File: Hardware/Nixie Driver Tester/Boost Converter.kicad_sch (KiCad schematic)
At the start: 6 parts, among them Q1 MMBT2222A, Q2 MMBT2907ALT1G, Q3 FDD7N25LZTM

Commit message: Switch mode 3.3V and SMD inductor
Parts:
- added C6: 100nF, Capacitor_SMD:C_0805_2012Metric, symbol Device:C
- L1: footprint Inductor_:Bourns RLB1014 -> Inductor_SMD:L_Wuerth_WE-PD-Typ-LS
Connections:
- net GND: now also C6.1
- net VBUS: now also C6.2
- net Gate Drive: now reaches Q1.2 (E), Q2.2 (E), Q3.1 (G)
- net Boost Src: now reaches D1.2 (A), L1.2, Q3.2 (D)
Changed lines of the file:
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@@
 	(paper "A4")
+	(junction
+		(at 93.98 58.42)
+		(diameter 0)
+		(color 0 0 0 0)
+	)
 	(junction
 		(at 101.6 88.9)
@@
 	)
 	(junction
-		(at 93.98 88.9)
+		(at 91.44 88.9)
 		(diameter 0)
 		(color 0 0 0 0)
@@
 	(wire
 		(pts
+			(xy 93.98 58.42) (xy 88.9 58.42)
+		)
+		(stroke
+			(width 0)
+			(type default)
+		)
+	)
+	(wire
+		(pts
 			(xy 101.6 88.9) (xy 111.76 88.9)
 		)
@@
 	(wire
 		(pts
+			(xy 93.98 40.64) (xy 93.98 43.18)
+		)
+		(stroke
+			(width 0)
+			(type default)
+		)
+	)
+	(wire
+		(pts
 			(xy 121.92 101.6) (xy 152.4 101.6)
 		)
@@
 	(wire
 		(pts
-			(xy 88.9 88.9) (xy 93.98 88.9)
-		)
-		(stroke
-			(width 0)
-			(type default)
-		)
-	)
-	(wire
-		(pts
-			(xy 93.98 88.9) (xy 93.98 101.6)
+			(xy 88.9 88.9) (xy 91.44 88.9)
+		)
+		(stroke
+			(width 0)
+			(type default)
+		)
+	)
+	(wire
+		(pts
+			(xy 91.44 88.9) (xy 91.44 101.6)
 		)
 		(stroke
@@
 	(wire
 		(pts
+			(xy 93.98 50.8) (xy 93.98 58.42)
+		)
+		(stroke
+			(width 0)
+			(type default)
+		)
+	)
+	(wire
+		(pts
 			(xy 101.6 63.5) (xy 101.6 71.12)
 		)
@@
 	(wire
 		(pts
-			(xy 106.68 58.42) (xy 88.9 58.42)
+			(xy 106.68 58.42) (xy 93.98 58.42)
 		)
 		(stroke
@@
 	(wire
 		(pts
-			(xy 93.98 88.9) (xy 93.98 76.2)
-		)
-		(stroke
-			(width 0)
-			(type default)
+			(xy 91.44 101.6) (xy 93.98 101.6)
+		)
+		(stroke
+			(width 0)
+			(type default)
+		)
+	)
+	(wire
+		(pts
+			(xy 91.44 88.9) (xy 91.44 76.2)
+		)
+		(stroke
+			(width 0)
+			(type default)
+		)
+	)
+	(wire
+		(pts
+			(xy 91.44 76.2) (xy 93.98 76.2)
+		)
+		(stroke
+			(width 0)
+			(type default)
+		)
+	)
+	(label "Gate Drive"
+		(at 101.6 93.98 0)
+		(effects
+			(font
+				(size 1.27 1.27)
+			)
+			(justify left bottom)
+		)
+	)
+	(label "Boost Src"
+		(at 121.92 68.58 0)
+		(effects
+			(font
+				(size 1.27 1.27)
+			)
+			(justify left bottom)
 		)
 	)
@@
 		(dnp no)
 		(fields_autoplaced yes)
-		(property "Reference" "#PWR04"
+		(property "Reference" "#PWR06"
 			(at 101.6 113.03 0)
 			(hide yes)
@@
 			(project "Nixie Driver Tester"
 				(path "/c2082ee6-4c2e-4b3c-b2d7-410eae192cfe/f65193b1-af2e-4613-8eac-c37ef85f5db5"
-					(reference "#PWR04")
+					(reference "#PWR06")
 					(unit 1)
 				)
@@
 		(dnp no)
 		(fields_autoplaced yes)
-		(property "Reference" "#PWR06"
+		(property "Reference" "#PWR07"
 			(at 121.92 113.03 0)
 			(hide yes)
@@
 			(project "Nixie Driver Tester"
 				(path "/c2082ee6-4c2e-4b3c-b2d7-410eae192cfe/f65193b1-af2e-4613-8eac-c37ef85f5db5"
-					(reference "#PWR06")
+					(reference "#PWR07")
+					(unit 1)
+				)
+			)
+		)
+	)
+	(symbol
+		(lib_id "Device:C")
+		(at 93.98 46.99 0)
+		(unit 1)
+		(body_style 1)
+		(exclude_from_sim no)
+		(in_bom yes)
+		(on_board yes)
+		(in_pos_files yes)
+		(dnp no)
+		(fields_autoplaced yes)
+		(property "Reference" "C6"
+			(at 97.79 45.7199 0)
+			(show_name no)
+			(do_not_autoplace no)
+			(effects
+				(font
+					(size 1.27 1.27)
+				)
+				(justify left)
+			)
+		)
+		(property "Value" "100nF"
+			(at 97.79 48.2599 0)
+			(show_name no)
+			(do_not_autoplace no)
+			(effects
+				(font
+					(size 1.27 1.27)
+				)
+				(justify left)
+			)
+		)
+		(property "Footprint" "Capacitor_SMD:C_0805_2012Metric"
+			(at 94.9452 50.8 0)
+			(hide yes)
+			(show_name no)
+			(do_not_autoplace no)
+			(effects
+				(font
+					(size 1.27 1.27)
+				)
+			)
+		)
+		(property "Datasheet" ""
+			(at 93.98 46.99 0)
+			(hide yes)
+			(show_name no)
+			(do_not_autoplace no)
+			(effects
+				(font
+					(size 1.27 1.27)
+				)
+			)
+		)
+		(property "Description" "Unpolarized capacitor"
+			(at 93.98 46.99 0)
+			(hide yes)
+			(show_name no)
+			(do_not_autoplace no)
+			(effects
+				(font
+					(size 1.27 1.27)
+				)
+			)
+		)
+		(pin "1"
+		)
+		(pin "2"
+		)
+		(instances
+			(project "Nixie Driver Tester"
+				(path "/c2082ee6-4c2e-4b3c-b2d7-410eae192cfe/f65193b1-af2e-4613-8eac-c37ef85f5db5"
+					(reference "C6")
 					(unit 1)
 				)
@@
 			)
 		)
-		(property "Footprint" "Inductor_:Bourns RLB1014"
+		(property "Footprint" "Inductor_SMD:L_Wuerth_WE-PD-Typ-LS"
 			(at 110.49 58.42 0)
 			(hide yes)
@@
 					(unit 1)
 				)
+			)
+		)
+	)
+	(symbol
+		(lib_id "power:GND")
+		(at 93.98 40.64 180)
+		(unit 1)
+		(body_style 1)
+		(exclude_from_sim no)
+		(in_bom yes)
+		(on_board yes)
+		(in_pos_files yes)
+		(dnp no)
+		(fields_autoplaced yes)
+		(property "Reference" "#PWR026"
+			(at 93.98 34.29 0)
+			(hide yes)
+			(show_name no)
+			(do_not_autoplace no)
+			(effects
+				(font
+					(size 1.27 1.27)
+				)
+			)
+		)
+		(property "Value" "GND"
+			(at 93.98 35.56 0)
+			(show_name no)
+			(do_not_autoplace no)
+			(effects
+				(font
+					(size 1.27 1.27)
+				)
+			)
+		)
+		(property "Footprint" ""
+			(at 93.98 40.64 0)
+			(hide yes)
+			(show_name no)
+			(do_not_autoplace no)
+			(effects
+				(font
+					(size 1.27 1.27)
+				)
+			)
+		)
+		(property "Datasheet" ""
+			(at 93.98 40.64 0)
+			(hide yes)
+			(show_name no)
+			(do_not_autoplace no)
+			(effects
+				(font
+					(size 1.27 1.27)
+				)
+			)
+		)
+		(property "Description" "Power symbol creates a global label with name \"GND\" , ground"
+			(at 93.98 40.64 0)
+			(hide yes)
+			(show_name no)
+			(do_not_autoplace no)
+			(effects
+				(font
+					(size 1.27 1.27)
+				)
+			)
+		)
+		(pin "1"
+		)
+		(instances
+			(project "Nixie Driver Tester"
+				(path "/c2082ee6-4c2e-4b3c-b2d7-410eae192cfe/f65193b1-af2e-4613-8eac-c37ef85f5db5"
+					(reference "#PWR026")
+					(unit 1)
+				)

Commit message: Added test points
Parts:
- added TP3: PWM, TestPoint:TestPoint_Keystone_5015_Micro_Mini, symbol Connector:TestPoint
- added TP4: VNN, TestPoint:TestPoint_Keystone_5015_Micro_Mini, symbol Connector:TestPoint
- renumbered C6 to C2, C2 to C3
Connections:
- net 180V: now also TP4.1
- net PWM: now also TP3.1
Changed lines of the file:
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@@
 	(paper "A4")
+	(junction
+		(at 91.44 76.2)
+		(diameter 0)
+		(color 0 0 0 0)
+	)
 	(junction
 		(at 93.98 58.42)
@@
 	)
 	(symbol
+		(lib_id "Connector:TestPoint")
+		(at 152.4 58.42 0)
+		(unit 1)
+		(body_style 1)
+		(exclude_from_sim no)
+		(in_bom yes)
+		(on_board yes)
+		(in_pos_files yes)
+		(dnp no)
+		(property "Reference" "TP4"
+			(at 152.4 53.34 0)
+			(show_name no)
+			(do_not_autoplace no)
+			(effects
+				(font
+					(size 1.27 1.27)
+				)
+				(justify bottom)
+			)
+		)
+		(property "Value" "VNN"
+			(at 154.94 56.3879 0)
+			(hide yes)
+			(show_name no)
+			(do_not_autoplace no)
+			(effects
+				(font
+					(size 1.27 1.27)
+				)
+				(justify left)
+			)
+		)
+		(property "Footprint" "TestPoint:TestPoint_Keystone_5015_Micro_Mini"
+			(at 157.48 58.42 0)
+			(hide yes)
+			(show_name no)
+			(do_not_autoplace no)
+			(effects
+				(font
+					(size 1.27 1.27)
+				)
+			)
+		)
+		(property "Datasheet" ""
+			(at 157.48 58.42 0)
+			(hide yes)
+			(show_name no)
+			(do_not_autoplace no)
+			(effects
+				(font
+					(size 1.27 1.27)
+				)
+			)
+		)
+		(property "Description" "test point"
+			(at 152.4 58.42 0)
+			(hide yes)
+			(show_name no)
+			(do_not_autoplace no)
+			(effects
+				(font
+					(size 1.27 1.27)
+				)
+			)
+		)
+		(pin "1"
+		)
+		(instances
+			(project "Nixie Driver Tester"
+				(path "/c2082ee6-4c2e-4b3c-b2d7-410eae192cfe/f65193b1-af2e-4613-8eac-c37ef85f5db5"
+					(reference "TP4")
+					(unit 1)
+				)
+			)
+		)
+	)
+	(symbol
 		(lib_id "Device:D_Schottky")
 		(at 130.81 58.42 180)
@@
 		(dnp no)
 		(fields_autoplaced yes)
-		(property "Reference" "#PWR06"
+		(property "Reference" "#PWR07"
 			(at 101.6 113.03 0)
 			(hide yes)
@@
 			(project "Nixie Driver Tester"
 				(path "/c2082ee6-4c2e-4b3c-b2d7-410eae192cfe/f65193b1-af2e-4613-8eac-c37ef85f5db5"
-					(reference "#PWR06")
+					(reference "#PWR07")
 					(unit 1)
 				)
@@
 		(dnp no)
 		(fields_autoplaced yes)
-		(property "Reference" "C2"
+		(property "Reference" "C3"
 			(at 156.21 87.6299 0)
 			(show_name no)
@@
 			(project "Nixie Driver Tester"
 				(path "/c2082ee6-4c2e-4b3c-b2d7-410eae192cfe/f65193b1-af2e-4613-8eac-c37ef85f5db5"
-					(reference "C2")
+					(reference "C3")
 					(unit 1)
 				)
@@
 		(dnp no)
 		(fields_autoplaced yes)
-		(property "Reference" "#PWR07"
+		(property "Reference" "#PWR08"
 			(at 121.92 113.03 0)
 			(hide yes)
@@
 			(project "Nixie Driver Tester"
 				(path "/c2082ee6-4c2e-4b3c-b2d7-410eae192cfe/f65193b1-af2e-4613-8eac-c37ef85f5db5"
-					(reference "#PWR07")
+					(reference "#PWR08")
 					(unit 1)
 				)
@@
 		(dnp no)
 		(fields_autoplaced yes)
-		(property "Reference" "C6"
+		(property "Reference" "C2"
 			(at 97.79 45.7199 0)
 			(show_name no)
@@
 			(project "Nixie Driver Tester"
 				(path "/c2082ee6-4c2e-4b3c-b2d7-410eae192cfe/f65193b1-af2e-4613-8eac-c37ef85f5db5"
-					(reference "C6")
+					(reference "C2")
 					(unit 1)
 				)
@@
 	)
 	(symbol
+		(lib_id "Connector:TestPoint")
+		(at 91.44 76.2 0)
+		(unit 1)
+		(body_style 1)
+		(exclude_from_sim no)
+		(in_bom yes)
+		(on_board yes)
+		(in_pos_files yes)
+		(dnp no)
+		(property "Reference" "TP3"
+			(at 91.44 71.12 0)
+			(show_name no)
+			(do_not_autoplace no)
+			(effects
+				(font
+					(size 1.27 1.27)
+				)
+				(justify bottom)
+			)
+		)
+		(property "Value" "PWM"
+			(at 93.98 74.1679 0)
+			(hide yes)
+			(show_name no)
+			(do_not_autoplace no)
+			(effects
+				(font
+					(size 1.27 1.27)
+				)
+				(justify left)
+			)
+		)
+		(property "Footprint" "TestPoint:TestPoint_Keystone_5015_Micro_Mini"
+			(at 96.52 76.2 0)
+			(hide yes)
+			(show_name no)
+			(do_not_autoplace no)
+			(effects
+				(font
+					(size 1.27 1.27)
+				)
+			)
+		)
+		(property "Datasheet" ""
+			(at 96.52 76.2 0)
+			(hide yes)
+			(show_name no)
+			(do_not_autoplace no)
+			(effects
+				(font
+					(size 1.27 1.27)
+				)
+			)
+		)
+		(property "Description" "test point"
+			(at 91.44 76.2 0)
+			(hide yes)
+			(show_name no)
+			(do_not_autoplace no)
+			(effects
+				(font
+					(size 1.27 1.27)
+				)
+			)
+		)
+		(pin "1"
+		)
+		(instances
+			(project "Nixie Driver Tester"
+				(path "/c2082ee6-4c2e-4b3c-b2d7-410eae192cfe/f65193b1-af2e-4613-8eac-c37ef85f5db5"
+					(reference "TP3")
+					(unit 1)
+				)
+			)
+		)
+	)
+	(symbol
 		(lib_id "power:GND")
 		(at 93.98 40.64 180)
@@
 		(dnp no)
 		(fields_autoplaced yes)
-		(property "Reference" "#PWR026"
+		(property "Reference" "#PWR06"
 			(at 93.98 34.29 0)
 			(hide yes)
@@
 			(project "Nixie Driver Tester"
 				(path "/c2082ee6-4c2e-4b3c-b2d7-410eae192cfe/f65193b1-af2e-4613-8eac-c37ef85f5db5"
-					(reference "#PWR026")
+					(reference "#PWR06")
 					(unit 1)
 				)

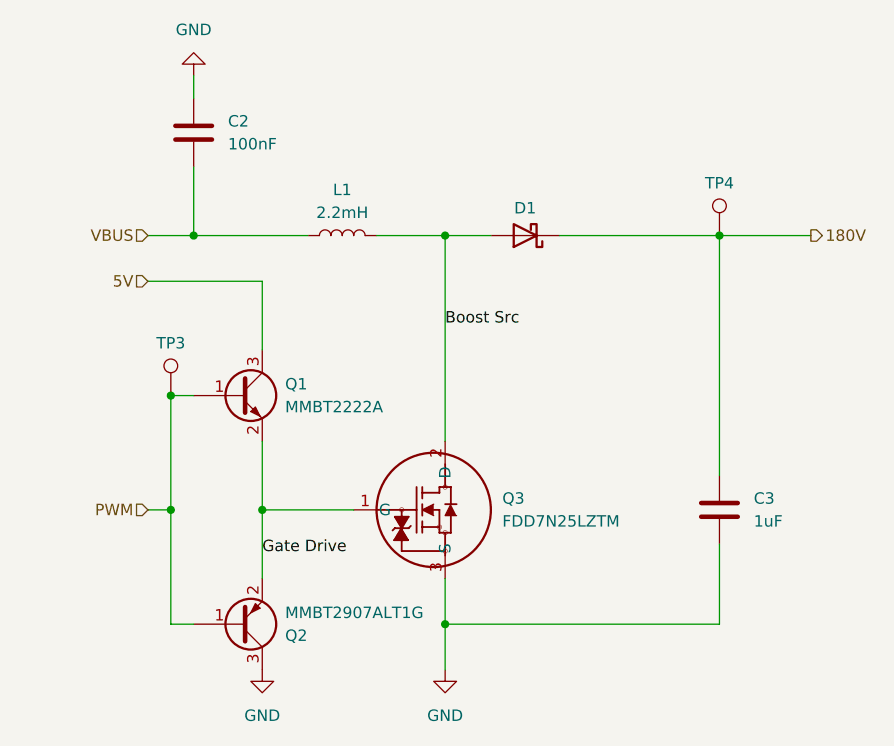
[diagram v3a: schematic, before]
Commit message: New MOSFET and driver IC
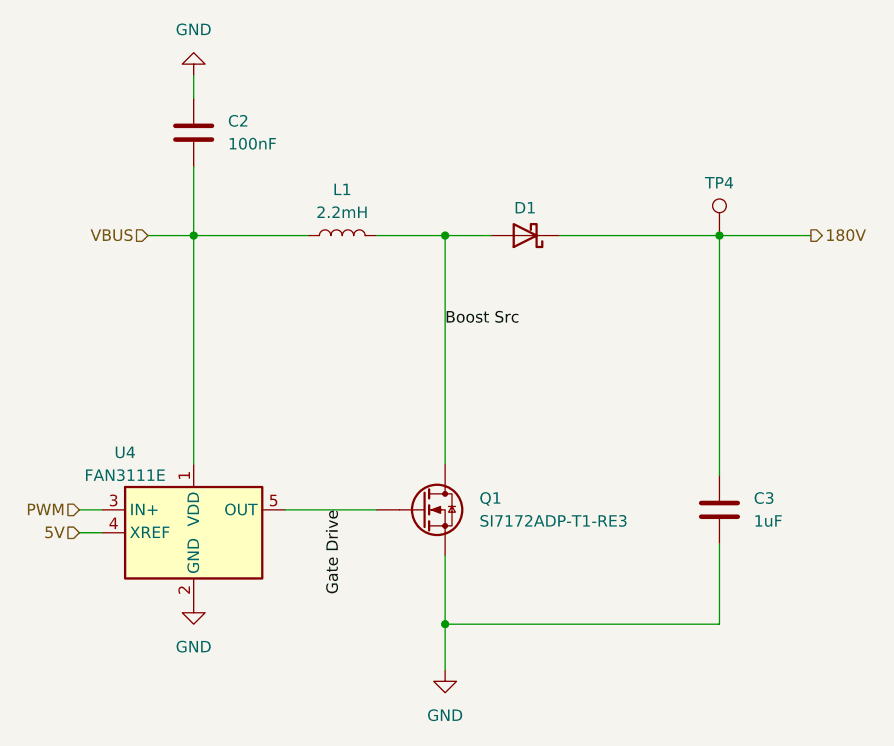
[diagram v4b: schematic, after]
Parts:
- removed Q1: MMBT2222A, Package_TO_SOT_SMD:SOT-23, symbol Device:Q_NPN_BEC
- removed Q2: MMBT2907ALT1G, Package_TO_SOT_SMD:SOT-23, symbol Device:Q_PNP_BEC
- removed Q3: FDD7N25LZTM, On Semi:DPAK_FDD7N_ONS, symbol Transistor_FET_:FDD7N25LZTM
- removed TP3: PWM, TestPoint:TestPoint_Keystone_5015_Micro_Mini, symbol Connector:TestPoint
- added Q1: SI7172ADP-T1-RE3, Package_SO:PowerPAK_SO-8_Single, symbol Device:Q_NMOS
- added U4: FAN3111E, Package_TO_SOT_SMD:SOT-23-5, symbol Driver_FET:FAN3111E
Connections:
- net 5V: now also U4.4 (XREF)
- net Boost Src: now also Q1.D
- net GND: now also Q1.S, U4.2 (GND)
- net Gate Drive: now also Q1.G, U4.5 (OUT)
- net PWM: now also U4.3 (IN+)
- net VBUS: now also U4.1 (VDD)

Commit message: switch MCU to SMT32C5
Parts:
- D1: value D_Schottky -> SMD220PL-TP
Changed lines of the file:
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@@
 			)
 		)
-		(property "Value" "D_Schottky"
+		(property "Value" "SMD220PL-TP"
 			(at 131.1275 54.61 0)
 			(hide yes)
